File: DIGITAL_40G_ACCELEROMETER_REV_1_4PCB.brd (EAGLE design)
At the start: 36.8 x 40.1 mm, 22 parts, among them IC1 ADIS16500AMLZ, IC2 LTC6820IUD#PBF, IC3 LDL1117S33R, T1 782482_33VC

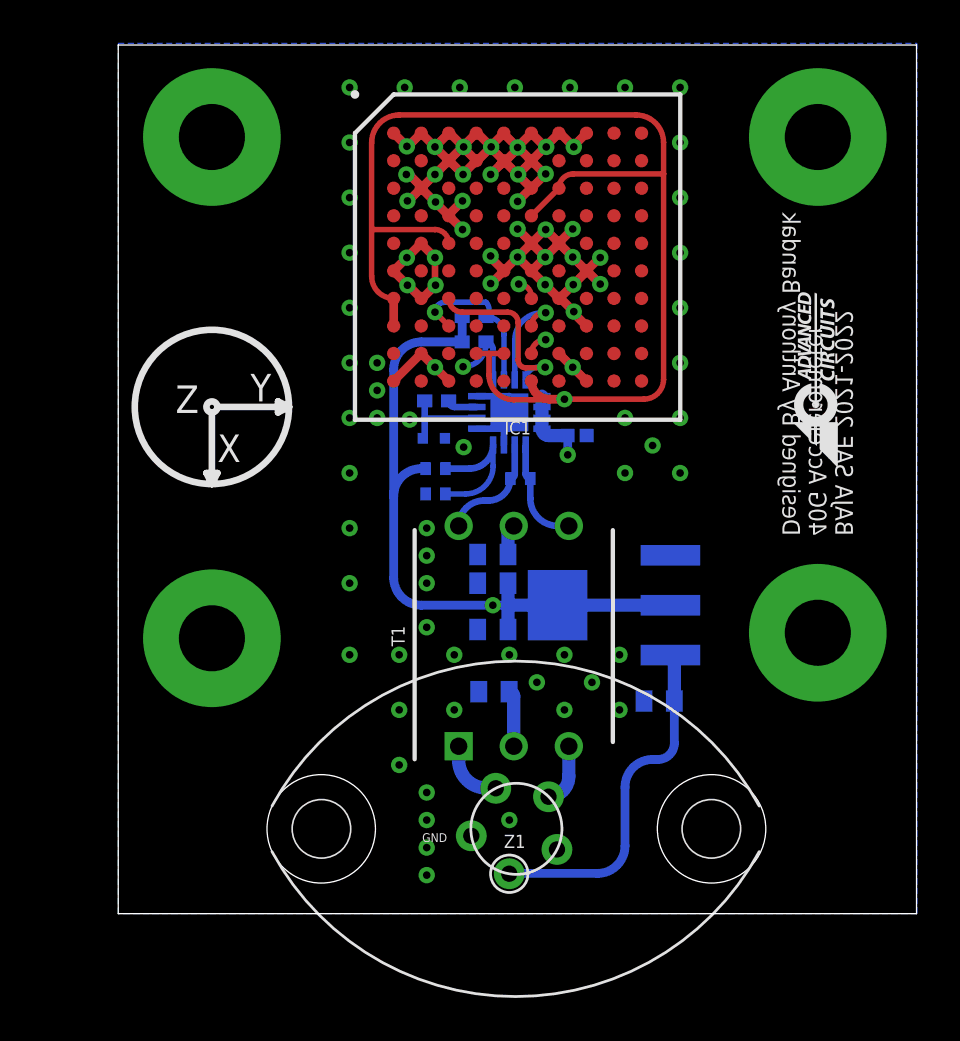
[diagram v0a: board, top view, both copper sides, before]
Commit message: Final final board layout update. Screw mounted now.
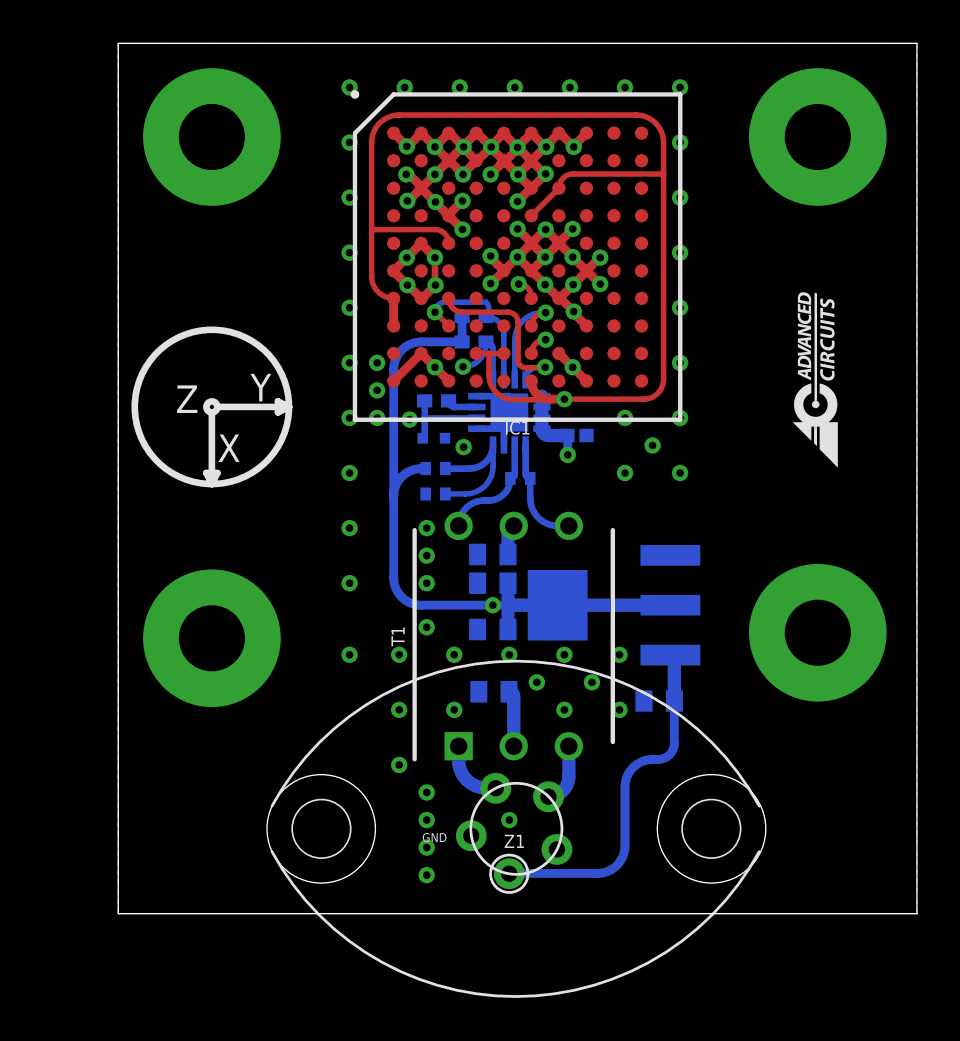
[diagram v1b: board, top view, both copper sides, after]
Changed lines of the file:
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@@
 </layers>
 <board>
-<fusionsync huburn="a.YnVzaW5lc3M6bXljcHA1NTk" projecturn="a.YnVzaW5lc3M6bXljcHA1NTkjRDIwMjEwOTE1NDQ0OTgwODU2" f3durn="urn:adsk.wipprod:dm.lineage:BeAIdd1JT46-xdl6n52ekA" pcbguid="" lastpulledtime="" lastsyncedchangeguid="" latestrevisionid="e2055030-3426-48bf-abe8-e574d661bf13" lastsyncedrevisionid="e2055030-3426-48bf-abe8-e574d661bf13" lastboardhashguid="ddb7343e-f448-0c2b-ff40-1aaefaed4244" lastpushedtime="2022-04-15T23:38:16Z" linktopcb3d="true"/>
+<fusionsync huburn="a.YnVzaW5lc3M6bXljcHA1NTk" projecturn="a.YnVzaW5lc3M6bXljcHA1NTkjRDIwMjEwOTE1NDQ0OTgwODU2" f3durn="urn:adsk.wipprod:dm.lineage:BeAIdd1JT46-xdl6n52ekA" pcbguid="" lastpulledtime="" lastsyncedchangeguid="" latestrevisionid="05985c92-ce82-46b7-9d4a-7c50af940576" lastsyncedrevisionid="05985c92-ce82-46b7-9d4a-7c50af940576" lastboardhashguid="b349df81-fa15-c74b-054d-e3d2b541b3e7" lastpushedtime="2022-04-16T00:49:16Z" linktopcb3d="true"/>
 <plain>
-<wire x1="0" y1="0" x2="36.81" y2="0" width="0" layer="20"/>
-<wire x1="36.81" y1="0" x2="36.81" y2="40.056" width="0" layer="20"/>
-<wire x1="36.81" y1="40.056" x2="0" y2="40.056" width="0" layer="20"/>
-<wire x1="0" y1="40.056" x2="0" y2="0" width="0" layer="20"/>
-<text x="30.624778125" y="17.42694375" size="0.8128" layer="25" rot="MR90">BAJA SAE 2021-2022
+<wire x1="0" y1="0" x2="36.83" y2="0" width="0" layer="20"/>
+<wire x1="36.83" y1="0" x2="36.83" y2="40.132" width="0" layer="20"/>
+<wire x1="36.83" y1="40.132" x2="0" y2="40.132" width="0" layer="20"/>
+<wire x1="0" y1="40.132" x2="0" y2="0" width="0" layer="20"/>
+<text x="28.3616375" y="17.42694375" size="0.8128" layer="26" rot="MR90">BAJA SAE 2021-2022
 40G Accelerometer
 Designed By Anthony Bandak</text>

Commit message: New layout. 2 layer board again. Updated 4PCB and regular version.
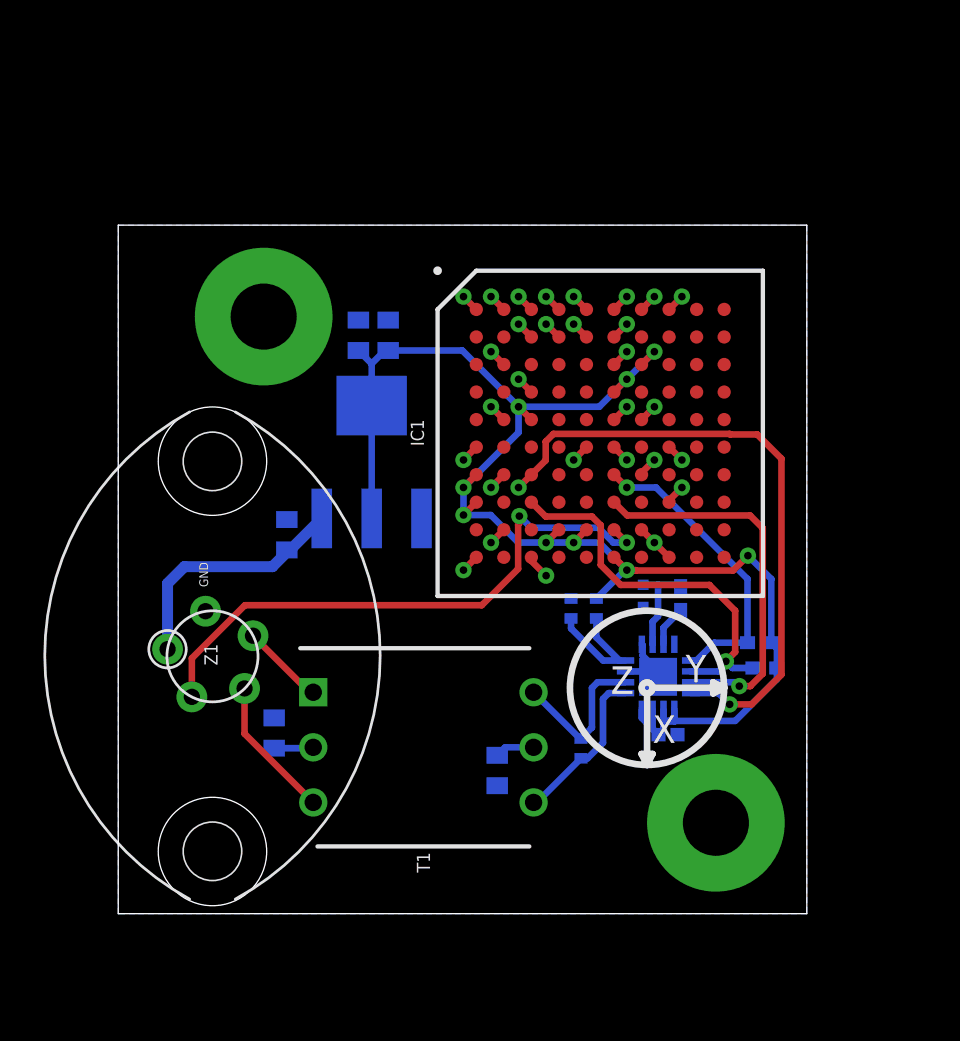
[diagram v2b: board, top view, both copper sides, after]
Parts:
- removed U$1, U$2: THROUGH_HOLE, SamacSys_Parts:1/16TH_BOLT
- moved U$3 26.9 mm to (6.71, 27.5), flipped to the bottom, turned to 180 degrees
- moved R13 21.0 mm to (29.8, 11.3), turned to 180 degrees
- moved R12 19.1 mm to (29.6, 12.5), turned to 180 degrees
- moved C1 18.8 mm to (7.77, 17.5), turned to 90 degrees
- moved Z1 16.0 mm to (4.39, 11.9), turned to 90 degrees
- moved C3 14.9 mm to (11.1, 26.7), turned to 90 degrees
- moved R14 14.5 mm to (25.9, 14.5), turned to 90 degrees
- moved C4 14.4 mm to (25.3, 8.26)
- moved IC2 14.0 mm to (24.9, 10.9), turned to 0 degrees
- moved IC3 13.0 mm to (11.7, 20.8), turned to 90 degrees
- moved R11 12.8 mm to (21.3, 7.62), turned to 90 degrees
- moved C2 12.4 mm to (12.4, 26.7), turned to 90 degrees
- moved R15 12.1 mm to (24.2, 14.7), turned to 90 degrees
- moved C5 10.3 mm to (7.19, 8.33), turned to 90 degrees
- moved C6 9.96 mm to (17.5, 6.60), turned to 270 degrees
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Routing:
- net GND: track 73.4 -> 29.1 mm, vias 90 -> 29
- net 3.3V: track 108.4 -> 70.0 mm, vias 3 -> 9
- net CS: track 7.94 -> 29.1 mm, vias 1 -> 2
- net SCK: track 4.69 -> 17.7 mm
- net MISO: track 7.36 -> 18.3 mm
- net DR: track 34.8 -> 27.3 mm, vias 1 -> 2
- net 12V: track 15.8 -> 11.4 mm
- net MOSI: track 10.0 -> 14.1 mm, vias 2 -> 1
- net IM: track 2.72 -> 6.57 mm
- net IMBOARD: track 4.86 -> 7.52 mm
- net IPBOARD: track 4.92 -> 7.27 mm
- net IP: track 2.90 -> 3.86 mm
- net N$2: track 2.60 -> 1.82 mm
- removed copper zone on layer 15, net GND
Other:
- board size 36.8 x 40.1 mm -> 31.8 x 31.8 mm
- board text added: "C:/Users/forre/Downloads/adv.bmp"
